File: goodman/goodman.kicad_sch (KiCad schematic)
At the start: 5 parts, among them J1 TSM-110-01-T-DV, J2 09561527613

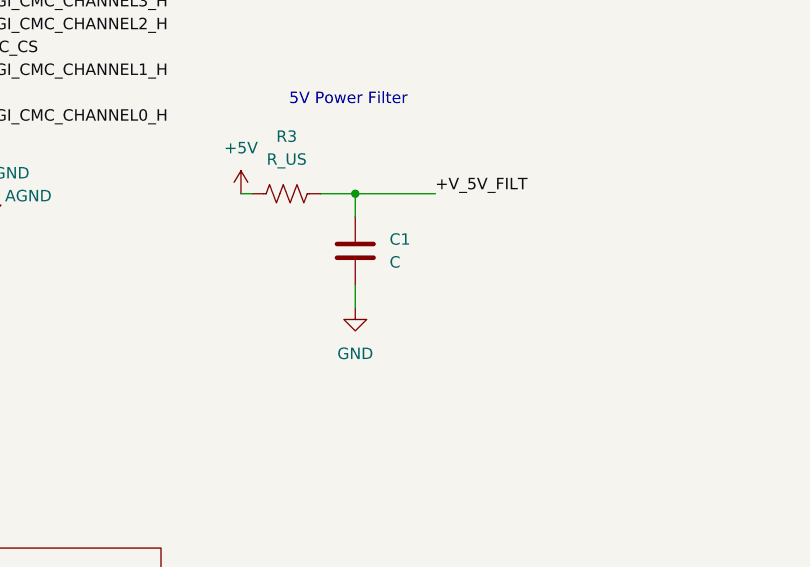
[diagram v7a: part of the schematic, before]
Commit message: Updated 5V power filter logic added another capacitor for high frequency noise
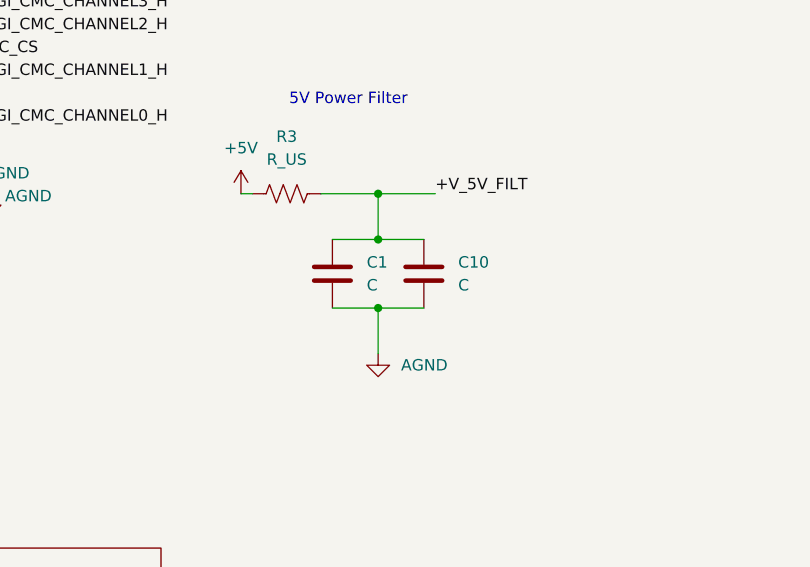
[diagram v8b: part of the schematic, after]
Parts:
- added C10: C, symbol Device:C
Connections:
- net GND is gone; now on net AGND: C1.2
- net +V_5V_FILT: now also C10.1
- net AGND: now also C10.2
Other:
- moved on the sheet: C1
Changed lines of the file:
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@@
+	)
+	(junction
+		(at 86.36 104.14)
+		(diameter 0)
+		(color 0 0 0 0)
 	)
 	(junction
@@
 	)
 	(junction
+		(at 86.36 109.22)
+		(diameter 0)
+		(color 0 0 0 0)
+	)
+	(junction
 		(at 162.56 93.98)
 		(diameter 0)
@@
 	)
 	(junction
-		(at 83.82 104.14)
-		(diameter 0)
-		(color 0 0 0 0)
-	)
-	(junction
 		(at 250.19 99.06)
 		(diameter 0)
@@
 	)
 	(junction
+		(at 86.36 116.84)
+		(diameter 0)
+		(color 0 0 0 0)
+	)
+	(junction
 		(at 38.1 109.22)
 		(diameter 0)
@@
 	(wire
 		(pts
+			(xy 86.36 104.14) (xy 86.36 109.22)
+		)
+		(stroke
+			(width 0)
+			(type default)
+		)
+	)
+	(wire
+		(pts
 			(xy 157.48 93.98) (xy 154.94 93.98)
 		)
@@
 	(wire
 		(pts
+			(xy 81.28 116.84) (xy 86.36 116.84)
+		)
+		(stroke
+			(width 0)
+			(type default)
+		)
+	)
+	(wire
+		(pts
 			(xy 252.73 93.98) (xy 250.19 93.98)
 		)
@@
 	(wire
 		(pts
-			(xy 83.82 104.14) (xy 92.71 104.14)
-		)
-		(stroke
-			(width 0)
-			(type default)
-		)
-	)
-	(wire
-		(pts
-			(xy 80.01 104.14) (xy 83.82 104.14)
+			(xy 80.01 104.14) (xy 86.36 104.14)
 		)
 		(stroke
@@
 	(wire
 		(pts
+			(xy 86.36 116.84) (xy 86.36 121.92)
+		)
+		(stroke
+			(width 0)
+			(type default)
+		)
+	)
+	(wire
+		(pts
 			(xy 34.29 68.58) (xy 38.1 68.58)
 		)
@@
 	(wire
 		(pts
+			(xy 86.36 116.84) (xy 91.44 116.84)
+		)
+		(stroke
+			(width 0)
+			(type default)
+		)
+	)
+	(wire
+		(pts
 			(xy 165.1 93.98) (xy 162.56 93.98)
 		)
@@
 	(wire
 		(pts
+			(xy 86.36 109.22) (xy 91.44 109.22)
+		)
+		(stroke
+			(width 0)
+			(type default)
+		)
+	)
+	(wire
+		(pts
 			(xy 176.53 76.2) (xy 180.34 76.2)
 		)
@@
 	(wire
 		(pts
+			(xy 81.28 109.22) (xy 86.36 109.22)
+		)
+		(stroke
+			(width 0)
+			(type default)
+		)
+	)
+	(wire
+		(pts
 			(xy 176.53 68.58) (xy 180.34 68.58)
 		)
@@
 	(wire
 		(pts
+			(xy 86.36 104.14) (xy 92.71 104.14)
+		)
+		(stroke
+			(width 0)
+			(type default)
+		)
+	)
+	(wire
+		(pts
 			(xy 250.19 91.44) (xy 250.19 93.98)
 		)
@@
 	(wire
 		(pts
-			(xy 83.82 104.14) (xy 83.82 106.68)
-		)
-		(stroke
-			(width 0)
-			(type default)
-		)
-	)
-	(wire
-		(pts
 			(xy 34.29 106.68) (xy 38.1 106.68)
 		)
@@
 		(pts
 			(xy 250.19 96.52) (xy 250.19 99.06)
-		)
-		(stroke
-			(width 0)
-			(type default)
-		)
-	)
-	(wire
-		(pts
-			(xy 83.82 116.84) (xy 83.82 114.3)
 		)
 		(stroke
@@
 	(symbol
 		(lib_id "Device:C")
-		(at 83.82 110.49 0)
+		(at 81.28 113.03 0)
 		(unit 1)
 		(body_style 1)
@@
 		(fields_autoplaced yes)
 		(property "Reference" "C1"
-			(at 87.63 109.2199 0)
+			(at 85.09 111.7599 0)
 			(show_name no)
 			(do_not_autoplace no)
@@
 		)
 		(property "Value" "C"
-			(at 87.63 111.7599 0)
+			(at 85.09 114.2999 0)
 			(show_name no)
 			(do_not_autoplace no)
@@
 		)
 		(property "Footprint" ""
-			(at 84.7852 114.3 0)
+			(at 82.2452 116.84 0)
 			(hide yes)
 			(show_name no)
@@
 		)
 		(property "Datasheet" ""
-			(at 83.82 110.49 0)
+			(at 81.28 113.03 0)
 			(hide yes)
 			(show_name no)
@@
 		)
 		(property "Description" "Unpolarized capacitor"
-			(at 83.82 110.49 0)
+			(at 81.28 113.03 0)
 			(hide yes)
 			(show_name no)
@@
 	(symbol
 		(lib_id "power:GND")
-		(at 83.82 116.84 0)
+		(at 86.36 121.92 0)
 		(unit 1)
 		(body_style 1)
@@
 		(fields_autoplaced yes)
 		(property "Reference" "#PWR018"
-			(at 83.82 123.19 0)
-			(hide yes)
-			(show_name no)
-			(do_not_autoplace no)
-			(effects
-				(font
-					(size 1.27 1.27)
-				)
-			)
-		)
-		(property "Value" "GND"
-			(at 83.82 121.92 0)
-			(show_name no)
-			(do_not_autoplace no)
-			(effects
-				(font
-					(size 1.27 1.27)
-				)
+			(at 86.36 128.27 0)
+			(hide yes)
+			(show_name no)
+			(do_not_autoplace no)
+			(effects
+				(font
+					(size 1.27 1.27)
+				)
+			)
+		)
+		(property "Value" "AGND"
+			(at 88.9 123.1899 0)
+			(show_name no)
+			(do_not_autoplace no)
+			(effects
+				(font
+					(size 1.27 1.27)
+				)
+				(justify left)
 			)
 		)
 		(property "Footprint" ""
-			(at 83.82 116.84 0)
+			(at 86.36 121.92 0)
 			(hide yes)
 			(show_name no)
@@
 		)
 		(property "Datasheet" ""
-			(at 83.82 116.84 0)
+			(at 86.36 121.92 0)
 			(hide yes)
 			(show_name no)
@@
 		)
 		(property "Description" "Power symbol creates a global label with name \"GND\" , ground"
-			(at 83.82 116.84 0)
+			(at 86.36 121.92 0)
 			(hide yes)
 			(show_name no)
@@
 					(unit 1)
 				)
+			)
+		)
+	)
+	(symbol
+		(lib_id "Device:C")
+		(at 91.44 113.03 0)
+		(unit 1)
+		(body_style 1)
+		(exclude_from_sim no)
+		(in_bom yes)
+		(on_board yes)
+		(in_pos_files yes)
+		(dnp no)
+		(fields_autoplaced yes)
+		(property "Reference" "C10"
+			(at 95.25 111.7599 0)
+			(show_name no)
+			(do_not_autoplace no)
+			(effects
+				(font
+					(size 1.27 1.27)
+				)
+				(justify left)
+			)
+		)
+		(property "Value" "C"
+			(at 95.25 114.2999 0)
+			(show_name no)
+			(do_not_autoplace no)
+			(effects
+				(font
+					(size 1.27 1.27)
+				)
+				(justify left)
+			)
+		)
+		(property "Footprint" ""
+			(at 92.4052 116.84 0)
+			(hide yes)
+			(show_name no)
+			(do_not_autoplace no)
+			(effects
+				(font
+					(size 1.27 1.27)
+				)
+			)
+		)
+		(property "Datasheet" ""
+			(at 91.44 113.03 0)
+			(hide yes)
+			(show_name no)
+			(do_not_autoplace no)
+			(effects
+				(font
+					(size 1.27 1.27)
+				)
+			)
+		)
+		(property "Description" "Unpolarized capacitor"
+			(at 91.44 113.03 0)
+			(hide yes)
+			(show_name no)
+			(do_not_autoplace no)
+			(effects
+				(font
+					(size 1.27 1.27)
+				)
+			)
+		)
+		(pin "1"
+		)
+		(pin "2"
+		)
+		(instances
+			(project "goodman"
+				(path "/52ec5281-98f9-4967-92c1-b39f2426ce6f"
+					(reference "C10")
+					(unit 1)
+				)
